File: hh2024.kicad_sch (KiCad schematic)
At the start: 62 parts, among them J1 SAO, J2 QWIIC, J3 Micro_SD_Card, J4 USB-C, J7 RELAY, K1 SANYOU_SRD_Form_C, Q3 AP2302B, SW1 Multi-Directional-Switches, SW2 Multi-Directional-Switches, SW3 Multi-Directional-Switches, SW4 Multi-Directional-Switches, SW5 Multi-Directional-Switches, U5 CH32V003F4U6, U6 74LVC1G125

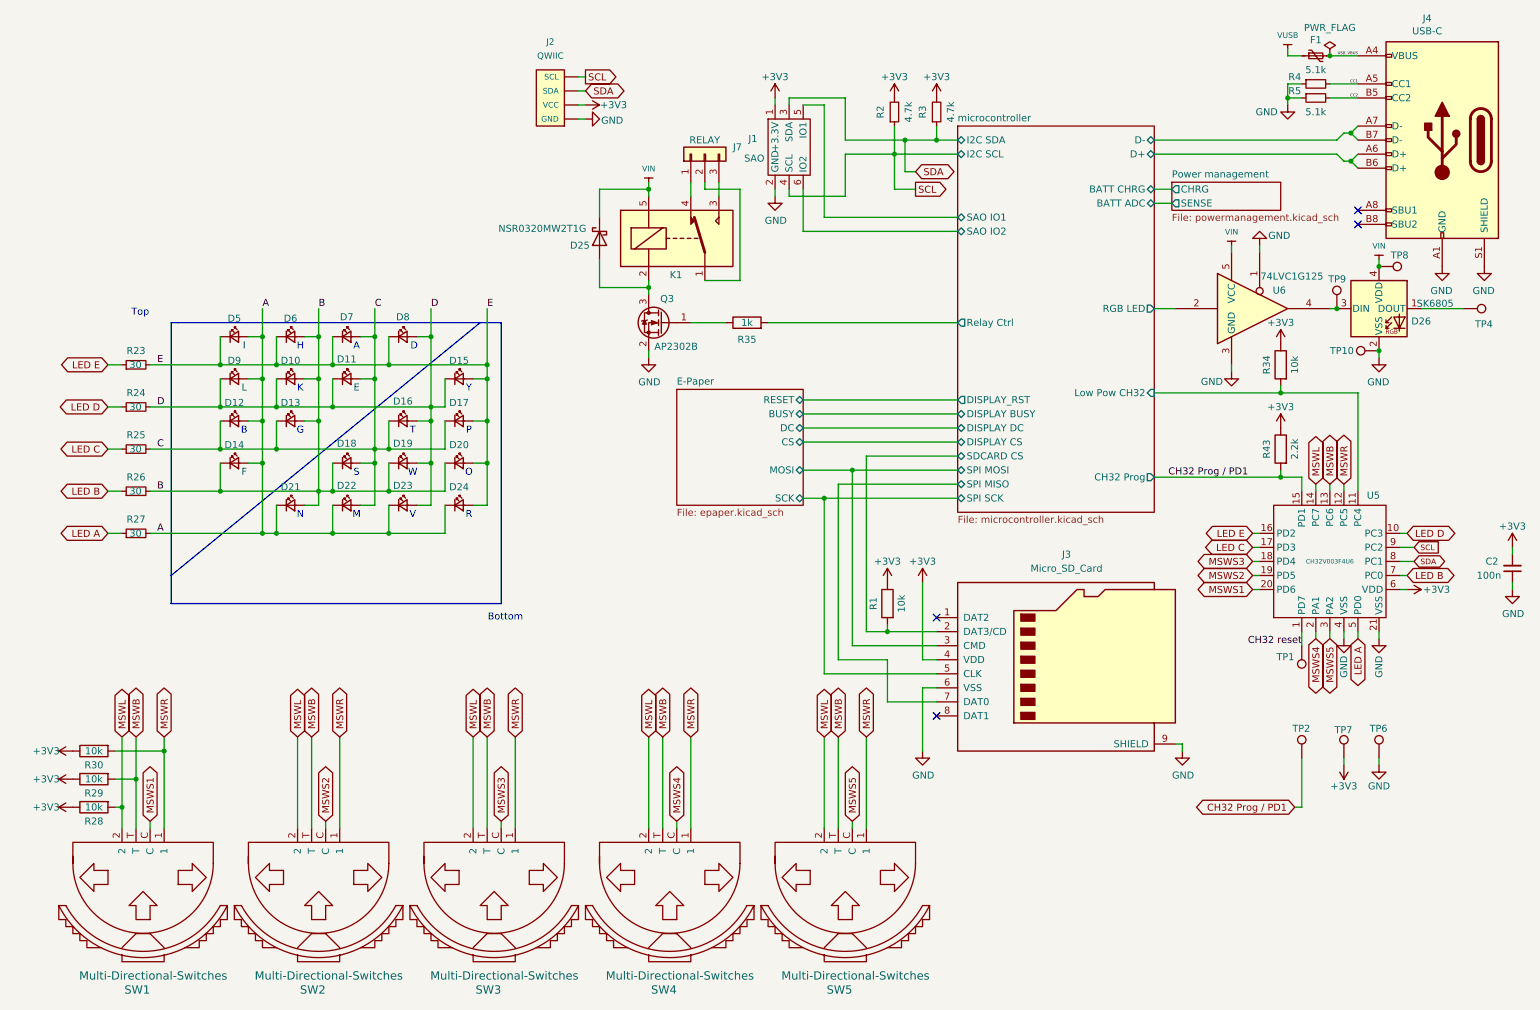
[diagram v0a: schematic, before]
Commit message: Added artwork (cont)
DRC pass
Removed header from the BoM
changed the relay header to SMD so it doesn't clash with art
made header for CH32 prog THT
Moved designators in reasonable place
added hacker hotel and badge.team artwork
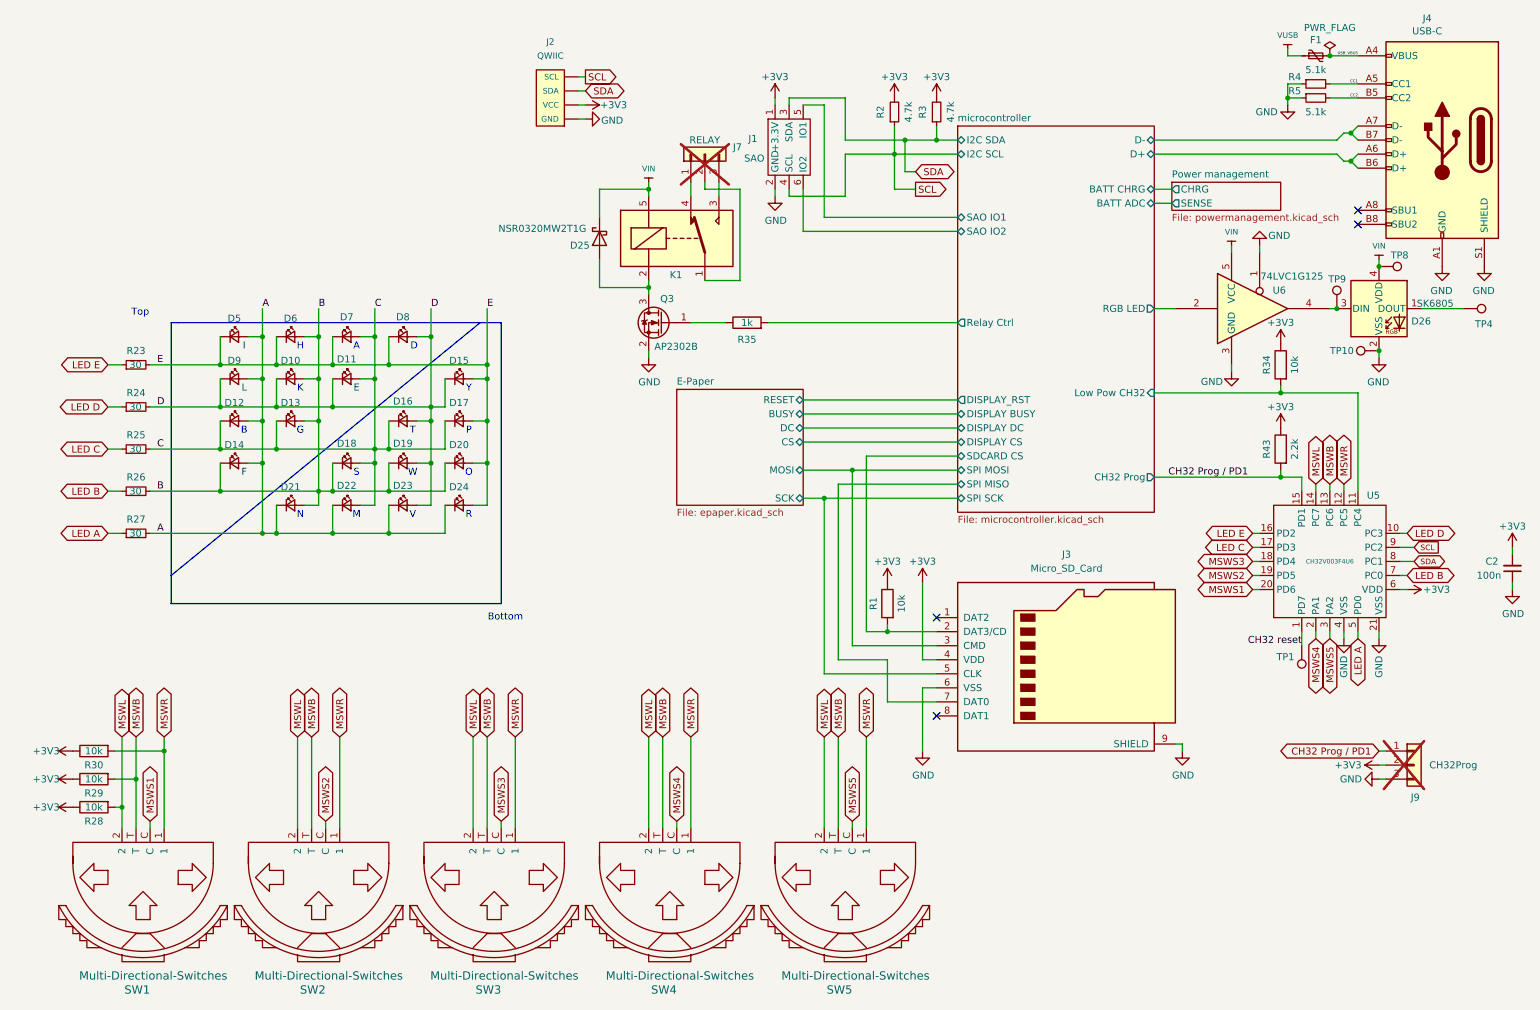
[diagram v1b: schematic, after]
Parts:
- removed TP2, TP6, TP7: TestPoint, TestPoint:TestPoint_Pad_2.0x2.0mm, symbol Connector:TestPoint
- added J9: CH32Prog, Connector_PinHeader_2.54mm:PinHeader_1x03_P2.54mm_Vertical, symbol Connector_Generic:Conn_01x03
- J7: footprint Connector_PinHeader_2.54mm:PinHeader_1x03_P2.54mm_Vertical -> Connector_PinHeader_2.54mm:PinHeader_1x03_P2.54mm_Vertical_SMD_Pin1Left; now not fitted; now left out of the parts list
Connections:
- net +3V3: now also J9.2 (Pin_2)
- net CH32 Prog / PD1: now also J9.1 (Pin_1)
- net GND: now also J9.3 (Pin_3)

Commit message: Moar headers
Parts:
- removed TP1, TP10, TP4, TP8, TP9: TestPoint, TestPoint:TestPoint_Pad_1.0x1.0mm, symbol Connector:TestPoint
- added J7: LED, Connector_PinHeader_2.54mm:PinHeader_1x04_P2.54mm_Vertical, symbol Connector_Generic:Conn_01x04
- J5: renamed from J9; footprint Connector_PinHeader_2.54mm:PinHeader_1x03_P2.54mm_Vertical -> Connector_PinHeader_2.54mm:PinHeader_2x02_P2.54mm_Vertical; symbol Connector_Generic:Conn_01x03 -> Connector_Generic:Conn_01x04; now in the parts list
- renumbered C2 to C1, D5 to D1, D11 to D10, D18 to D11, D22 to D12, D8 to D13, D16 to D14, D19 to D15, D23 to D16, D15 to D17, D17 to D18, D20 to D19, D9 to D2, D24 to D20, D25 to D21, D26 to D22, D12 to D3, D14 to D4, D6 to D5, D10 to D6, D13 to D7, D21 to D8, D7 to D9, J2 to J1, J7 to J2, J1 to J3, J3 to J4, J4 to J6, Q3 to Q1, R30 to R1, R1 to R10, R2 to R11, R3 to R12, R34 to R13, R43 to R14, R4 to R15, R5 to R16, R29 to R2, R28 to R3, R23 to R4, R24 to R5, R25 to R6, R26 to R7, R27 to R8, R35 to R9, U6 to U1, U5 to U2
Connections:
- net +3V3: now also J5.3 (Pin_3); no longer J5.2 (Pin_2)
- net CH32 Prog / PD1: now also J5.2 (Pin_2); no longer J5.1 (Pin_1)
- net CH32 reset: now also J5.1 (Pin_1)
- net GND: now also J5.4 (Pin_4), J7.4 (Pin_4); no longer J5.3 (Pin_3)
- net VIN: now also J7.3 (Pin_3)
- net at D22.1 (DOUT): now also J7.1 (Pin_1)
- net at D22.3 (DIN), U1.4: now also J7.2 (Pin_2)

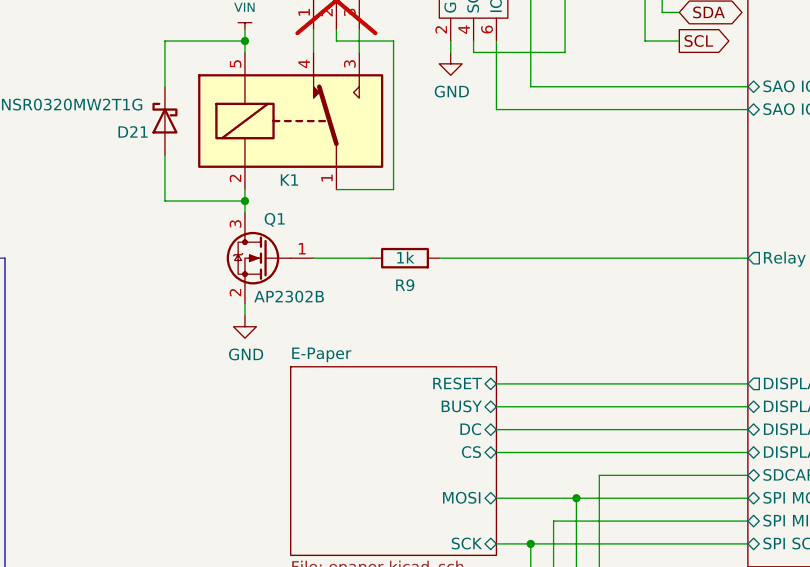
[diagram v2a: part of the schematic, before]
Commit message: tidy silk and solved DRC errors
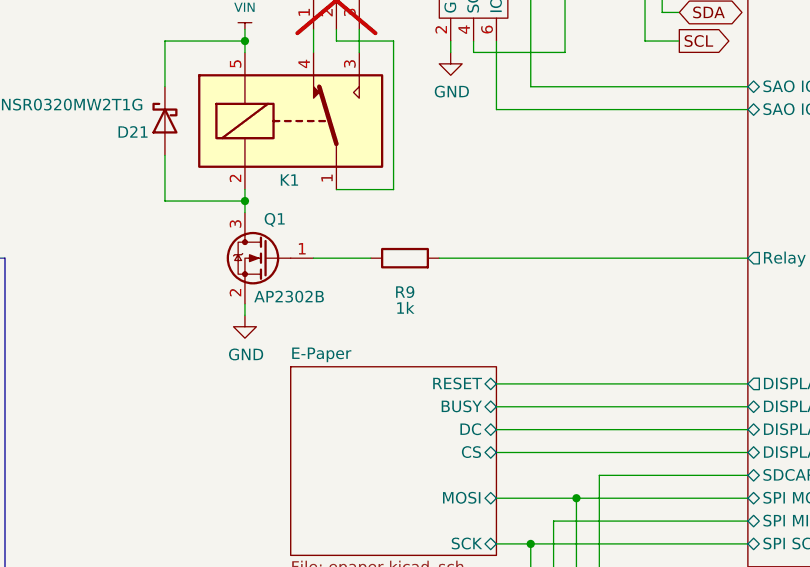
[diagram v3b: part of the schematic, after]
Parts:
- R14: LCSC (none) -> C114561; Link (none) -> https://www.lcsc.com/product-detail/Chip-Resistor-Surface-M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
- R9: Link https://www.lcsc.com/product-detail/Chip-span-style-background-color-ff0-Resistor-span-Surface-Mount_VO-SCR0805J1K_C3017842.html -> https://www.lcsc.com/product-detail/Chip-span-style-background-color-ff0-Resistor-span-Surface-Mount_VO-SCR0805J1K_C3017842.html
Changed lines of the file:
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@@
 			)
 		)
-		(property "Datasheet" ""
+		(property "Datasheet" "https://datasheet.lcsc.com/lcsc/2304140030_YAGEO-RC0805FR-072K2L_C114561.pdf"
 			(at 238.76 93.98 0)
 			(effects
@@
 			)
 		)
-		(property "LCSC" ""
+		(property "LCSC" "C114561"
 			(at 238.76 93.98 0)
 			(effects
@@
 			)
 		)
-		(property "Link" ""
+		(property "Link" "https://www.lcsc.com/product-detail/Chip-Resistor-Surface-Mount_YAGEO-RC0805FR-072K2L_C114561.html"
 			(at 238.76 93.98 0)
 			(effects
@@
 	)
 	(symbol
+		(lib_id "symbols:R")
+		(at 142.24 71.12 90)
+		(unit 1)
+		(exclude_from_sim no)
+		(in_bom yes)
+		(on_board yes)
+		(dnp no)
+		(property "Reference" "R9"
+			(at 142.24 74.93 90)
+			(effects
+				(font
+					(size 1.27 1.27)
+				)
+			)
+		)
+		(property "Value" "1k"
+			(at 142.24 76.708 90)
+			(effects
+				(font
+					(size 1.27 1.27)
+				)
+			)
+		)
+		(property "Footprint" "Resistor_SMD:R_0805_2012Metric"
+			(at 142.24 72.898 90)
+			(effects
+				(font
+					(size 1.27 1.27)
+				)
+				(hide yes)
+			)
+		)
+		(property "Datasheet" ""
+			(at 142.24 71.12 0)
+			(effects
+				(font
+					(size 1.27 1.27)
+				)
+				(hide yes)
+			)
+		)
+		(property "Description" ""
+			(at 142.24 71.12 0)
+			(effects
+				(font
+					(size 1.27 1.27)
+				)
+				(hide yes)
+			)
+		)
+		(property "LCSC" "C3017842"
+			(at 142.24 71.12 0)
+			(effects
+				(font
+					(size 1.27 1.27)
+				)
+				(hide yes)
+			)
+		)
+		(property "Buy early" ""
+			(at 142.24 71.12 0)
+			(effects
+				(font
+					(size 1.27 1.27)
+				)
+				(hide yes)
+			)
+		)
+		(property "Link" "https://www.lcsc.com/product-detail/Chip-span-style-background-color-ff0-Resistor-span-Surface-Mount_VO-SCR0805J1K_C3017842.html "
+			(at 142.24 71.12 0)
+			(effects
+				(font
+					(size 1.27 1.27)
+				)
+				(hide yes)
+			)
+		)
+		(property "Field-1" ""
+			(at 142.24 71.12 0)
+			(effects
+				(font
+					(size 1.27 1.27)
+				)
+				(hide yes)
+			)
+		)
+		(pin "1"
+		)
+		(pin "2"
+		)
+		(instances
+			(project "hh2024"
+				(path "/5f312b85-6822-40a3-b417-2df49696ca2d"
+					(reference "R9")
+					(unit 1)
+				)
+			)
+		)
+	)
+	(symbol
 		(lib_id "Device:LED_Small")
 		(at 80.01 96.52 0)
@@
 					(unit 1)
 				)
-			)
-		)
-	)
-	(symbol
-		(lib_id "symbols:R")
-		(at 142.24 71.12 90)
-		(unit 1)
-		(exclude_from_sim no)
-		(in_bom yes)
-		(on_board yes)
-		(dnp no)
-		(property "Reference" "R9"
-			(at 142.24 74.168 90)
-			(effects
-				(font
-					(size 1.27 1.27)
-				)
-			)
-		)
-		(property "Value" "1k"
-			(at 142.24 71.12 90)
-			(effects
-				(font
-					(size 1.27 1.27)
-				)
-			)
-		)
-		(property "Footprint" "Resistor_SMD:R_0805_2012Metric"
-			(at 142.24 72.898 90)
-			(effects
-				(font
-					(size 1.27 1.27)
-				)
-				(hide yes)
-			)
-		)
-		(property "Datasheet" "https://datasheet.lcsc.com/lcsc/2205131800_VO-SCR0805J1K_C3017842.pdf"
-			(at 142.24 71.12 0)
-			(effects
-				(font
-					(size 1.27 1.27)
-				)
-				(hide yes)
-			)
-		)
-		(property "Description" ""
-			(at 142.24 71.12 0)
-			(effects
-				(font
-					(size 1.27 1.27)
-				)
-				(hide yes)
-			)
-		)
-		(property "LCSC" "C3017842"
-			(at 142.24 71.12 0)
-			(effects
-				(font
-					(size 1.27 1.27)
-				)
-				(hide yes)
-			)
-		)
-		(property "Buy early" ""
-			(at 142.24 71.12 0)
-			(effects
-				(font
-					(size 1.27 1.27)
-				)
-				(hide yes)
-			)
-		)
-		(property "Link" "https://www.lcsc.com/product-detail/Chip-span-style-background-color-ff0-Resistor-span-Surface-Mount_VO-SCR0805J1K_C3017842.html"
-			(at 142.24 71.12 0)
-			(effects
-				(font
-					(size 1.27 1.27)
-				)
-				(hide yes)
-			)
-		)
-		(property "Field-1" ""
-			(at 142.24 71.12 0)
-			(effects
-				(font
-					(size 1.27 1.27)
-				)
-				(hide yes)
-			)
-		)
-		(pin "1"
-		)
-		(pin "2"
-		)
-		(instances
-			(project "hh2024"
-				(path "/5f312b85-6822-40a3-b417-2df49696ca2d"
-					(reference "R9")
-					(unit 1)
-				)

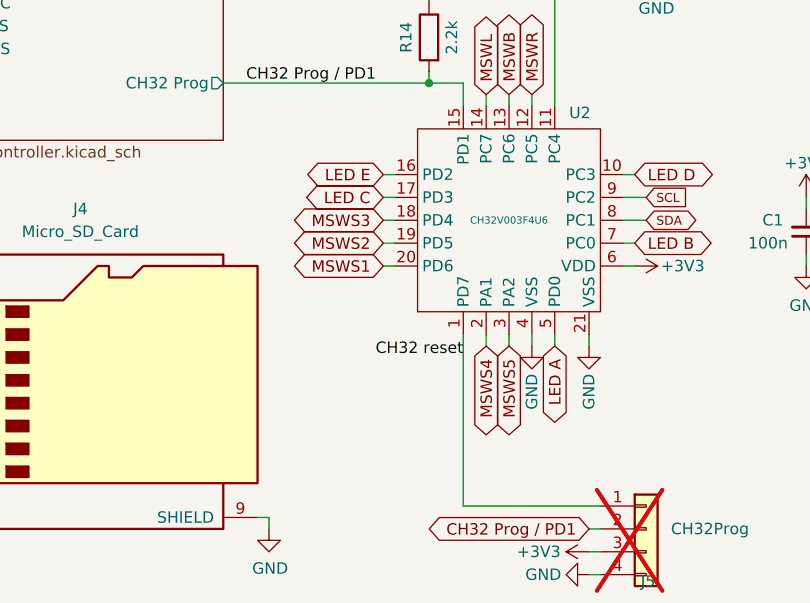
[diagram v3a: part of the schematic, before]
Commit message: V1.4
Swapped back PA1 and PA2 with PD3 and PD2 since Renze got them working
7 errors of copper which bleeds over edgecut
117 warning of soldermask bridging

generated bom, gerber, placement files and schematic
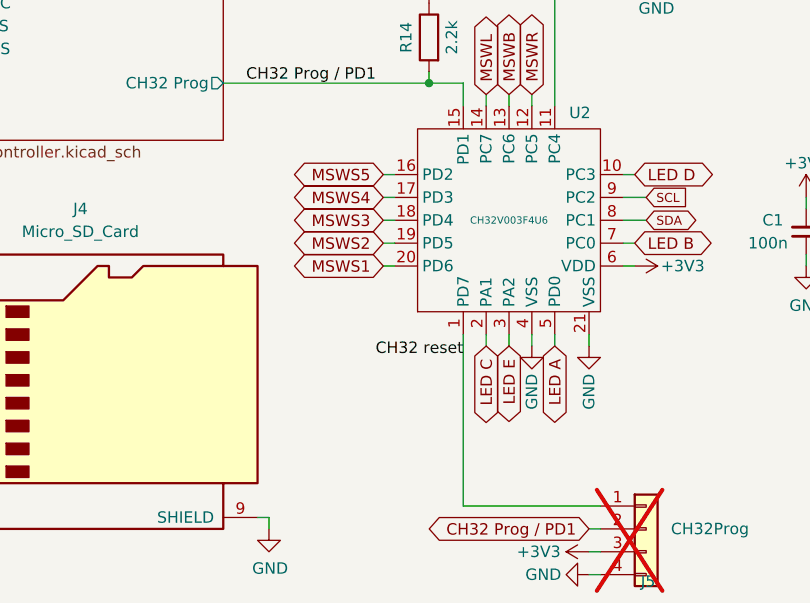
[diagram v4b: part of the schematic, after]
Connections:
- net LED C: now also U2.2 (PA1); no longer U2.17 (PD3)
- net LED E: now also U2.3 (PA2); no longer U2.16 (PD2)
- net MSWS4: now also U2.17 (PD3); no longer U2.2 (PA1)
- net MSWS5: now also U2.16 (PD2); no longer U2.3 (PA2)
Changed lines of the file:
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@@
 	(title_block
 		(title "HackerHotel 2024 badge")
-		(date "2023-12-15")
-		(rev "1.3")
+		(date "2023-12-17")
+		(rev "1.4")
 		(company "Nicolai Electronics & tilde.industries")
 		(comment 1 "License: CERN Open Hardware Licence Version 2 - Permissive")
@@
 	(global_label "LED C"
 		(shape bidirectional)
-		(at 233.68 111.76 180)
+		(at 245.11 128.27 270)
 		(fields_autoplaced yes)
 		(effects
@@
 		)
 		(property "Intersheetrefs" "${INTERSHEET_REFS}"
-			(at 225.8917 111.76 0)
+			(at 245.11 137.2382 90)
 			(effects
 				(font
@@
 	(global_label "MSWS4"
 		(shape bidirectional)
-		(at 245.11 128.27 270)
+		(at 233.68 111.76 180)
 		(fields_autoplaced yes)
 		(effects
@@
 		)
 		(property "Intersheetrefs" "${INTERSHEET_REFS}"
-			(at 245.11 137.5671 90)
+			(at 223.8652 111.76 0)
 			(effects
 				(font
@@
 	(global_label "MSWS5"
 		(shape bidirectional)
-		(at 247.65 128.27 270)
+		(at 233.68 109.22 180)
 		(fields_autoplaced yes)
 		(effects
@@
 		)
 		(property "Intersheetrefs" "${INTERSHEET_REFS}"
-			(at 247.65 137.5671 90)
+			(at 223.8652 109.22 0)
 			(effects
 				(font
@@
 	(global_label "LED E"
 		(shape bidirectional)
-		(at 233.68 109.22 180)
+		(at 247.65 128.27 270)
 		(fields_autoplaced yes)
 		(effects
@@
 		)
 		(property "Intersheetrefs" "${INTERSHEET_REFS}"
-			(at 226.0381 109.22 0)
+			(at 247.65 137.1172 90)
 			(effects
 				(font
